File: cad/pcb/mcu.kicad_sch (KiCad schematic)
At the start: 30 parts, among them X3 SWD-Conn, Y1 32.768k, Y2 32MHz

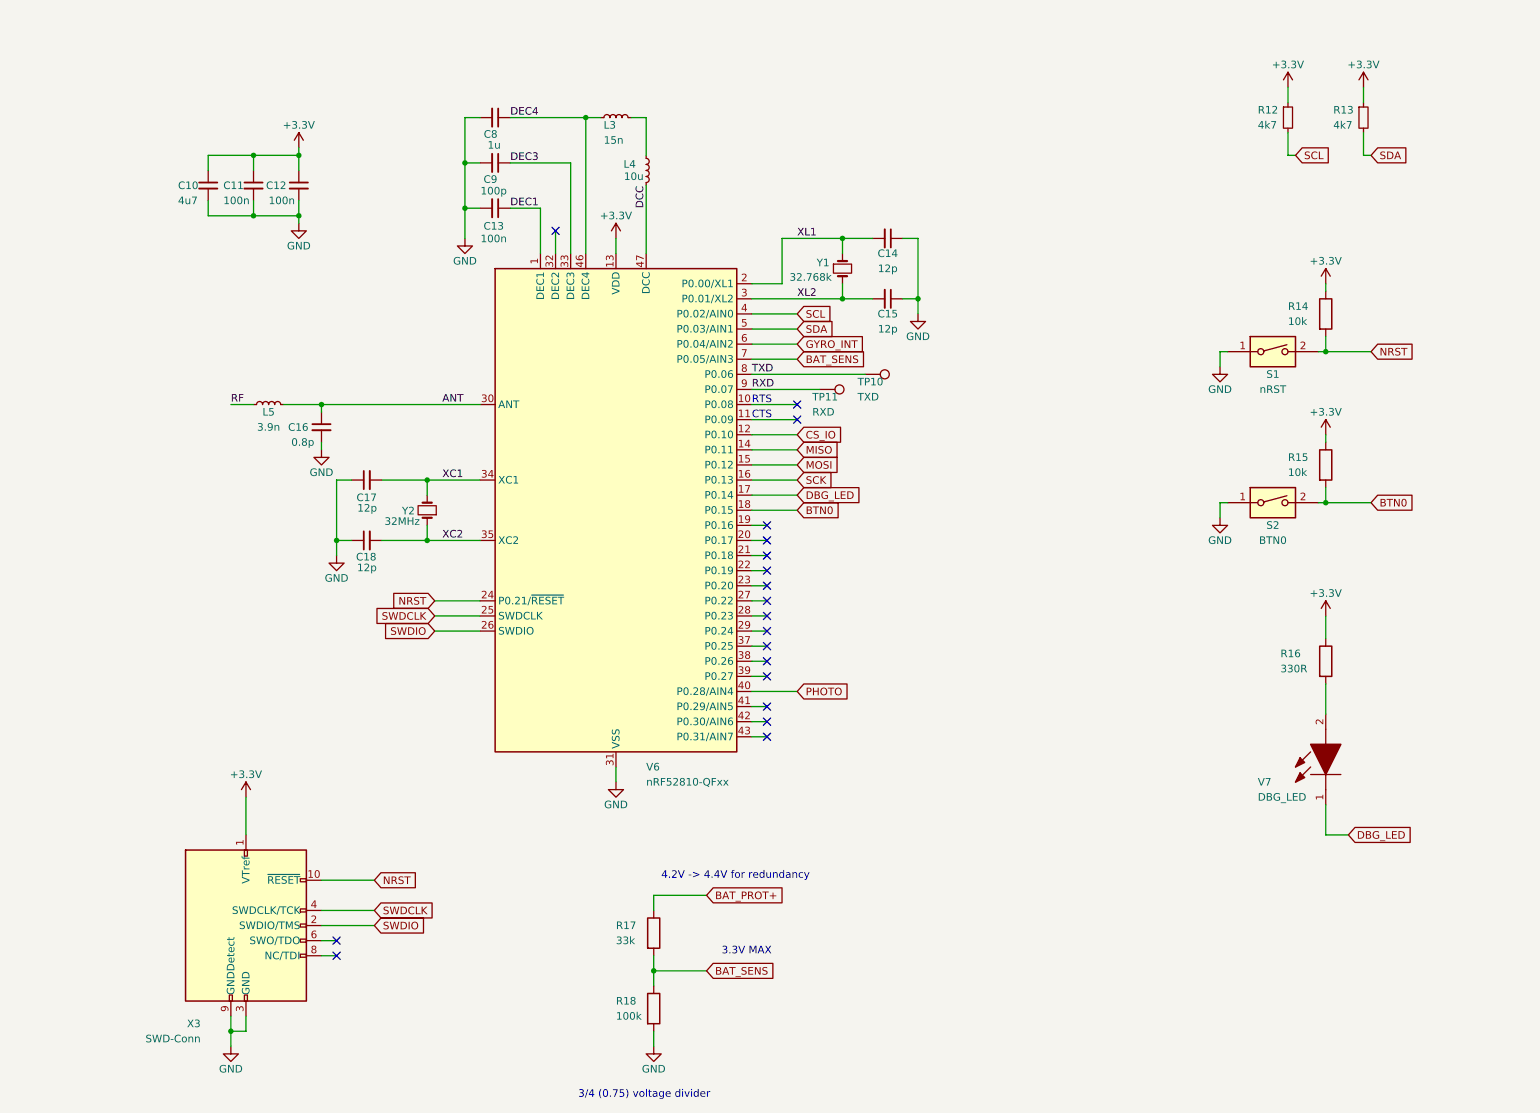
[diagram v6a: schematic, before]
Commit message: add usb-c footprint
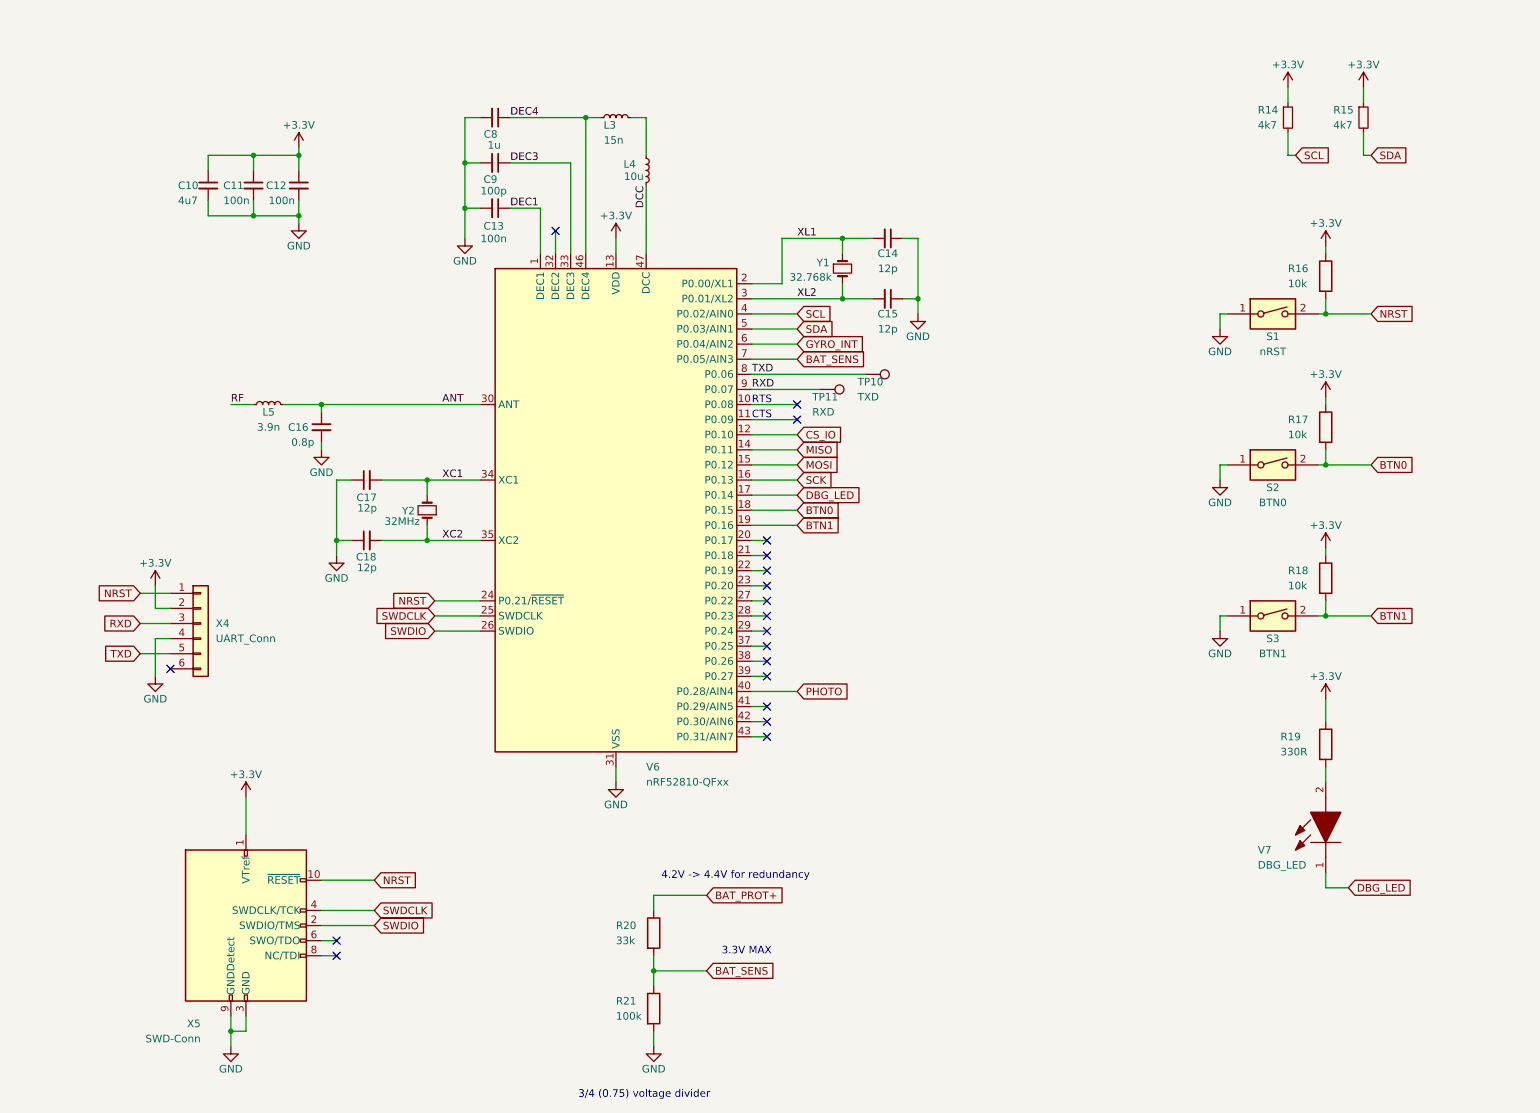
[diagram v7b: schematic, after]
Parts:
- added R18: 10k, symbol Device:R
- added S3: BTN1, symbol Switch:SW_DIP_x01
- added X4: UART_Conn, symbol Connector_Generic:Conn_01x06
- renumbered R12 to R14, R13 to R15, R14 to R16, R15 to R17, R16 to R19, R17 to R20, R18 to R21, X3 to X5
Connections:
- net +3.3V: now also R18.1, X4.2 (Pin_2)
- net GND: now also S3.1, X4.4 (Pin_4)
- net NRST: now also X4.1 (Pin_1)
- net RXD: now also X4.3 (Pin_3)
- net TXD: now also X4.5 (Pin_5)
- net BTN1: now reaches V6.19 (P0.16)
- net BTN1: now also R18.2, S3.2
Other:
- moved on the sheet: R16, R17, R19, S1, S2, V7

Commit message: generate bom; select C's & L's
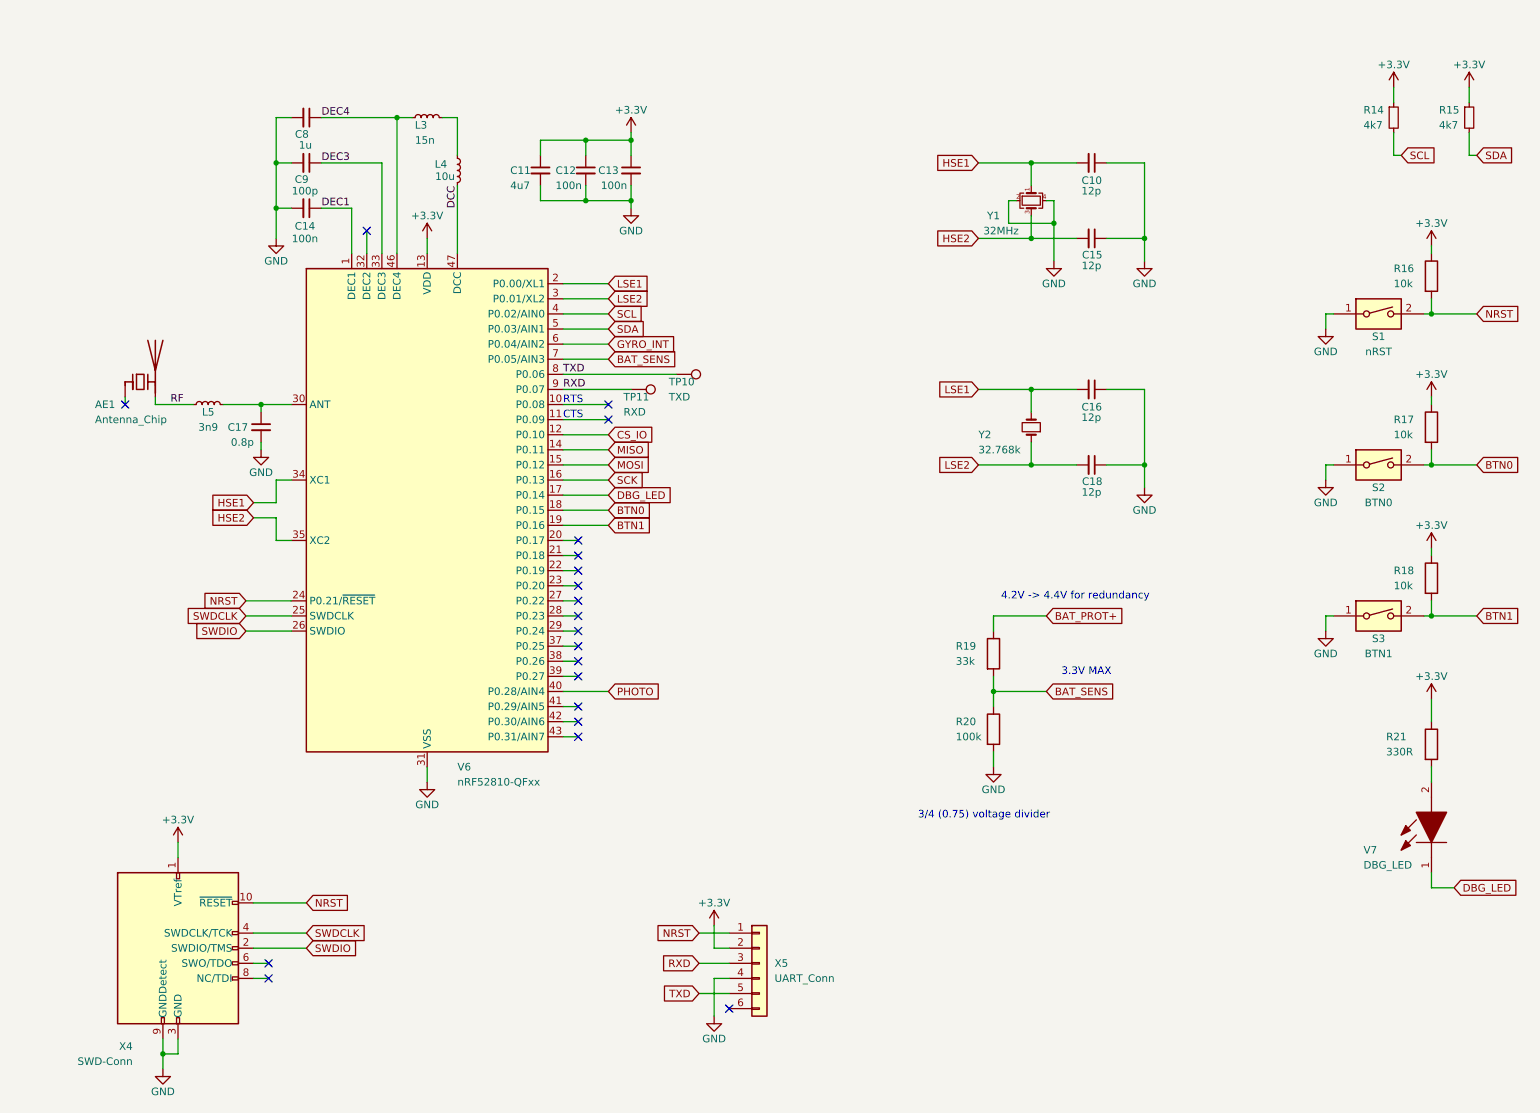
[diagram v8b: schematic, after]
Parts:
- removed C14, C17: 12p, symbol Device:C_Small
- removed Y1: 32.768k, symbol Device:Crystal_Small
- added AE1: Antenna_Chip, myLib:Ignion_NN01-102_BT_WIFI, symbol Device:Antenna_Chip
- added C10, C16: 12p, Capacitor_SMD:C_0603_1608Metric, symbol Device:C_Small
- added Y1: 32MHz, Crystal:Crystal_SMD_2520-4Pin_2.5x2.0mm, symbol Device:Crystal_GND24_Small
- C11: renamed from C10; footprint (none) -> Capacitor_SMD:C_0603_1608Metric
- C12: renamed from C11; footprint (none) -> Capacitor_SMD:C_0603_1608Metric
- C13: renamed from C12; footprint (none) -> Capacitor_SMD:C_0603_1608Metric
- C14: renamed from C13; footprint (none) -> Capacitor_SMD:C_0603_1608Metric
- C15, C18, C8, C9: footprint (none) -> Capacitor_SMD:C_0603_1608Metric
- C17: renamed from C16; footprint (none) -> Capacitor_SMD:C_0603_1608Metric
- L3, L4: footprint (none) -> Inductor_SMD:L_0603_1608Metric
- L5: value 3.9n -> 3n9; footprint (none) -> Inductor_SMD:L_0603_1608Metric
- R14, R15, R16, R17, R18: footprint (none) -> Resistor_SMD:R_0603_1608Metric
- R19: renamed from R20; footprint (none) -> Resistor_SMD:R_0603_1608Metric
- R20: renamed from R21; footprint (none) -> Resistor_SMD:R_0603_1608Metric
- R21: renamed from R19; footprint (none) -> Resistor_SMD:R_0603_1608Metric
- S1, S2, S3: footprint (none) -> Button_Switch_SMD:SW_SPST_CK_RS282G05A3
- TP10, TP11: footprint (none) -> TestPoint:TestPoint_Pad_D1.0mm
- V6: Mouser Part Number (none) -> 949-NRF52810-QFAA-T
- X5: renamed from X4; footprint (none) -> Connector_PinHeader_1.27mm:PinHeader_2x03_P1.27mm_Vertical_SMD
- Y2: value 32MHz -> 32.768k; footprint (none) -> Crystal:Crystal_SMD_3215-2Pin_3.2x1.5mm; Mouser Part Number (none) -> ECS-.327-9-34B-C-TR
- renumbered X5 to X4
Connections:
- net GND: now also C10.1, C16.1, Y1.2, Y1.4
- net RF: now also AE1.2 (PCB_Trace)
- net ANT: no longer names the net of C17.1, L5.2, V6.30 (ANT)
- net XC1 renamed HSE1
- net HSE1: now also C10.2, Y1.1; no longer Y2.2
- net XC2 renamed LSE2
- net LSE2: now also V6.3 (P0.01/XL2); no longer V6.35 (XC2)
- net XL1 renamed LSE1
- net LSE1: now also Y2.2, C16.2
- net XL2 renamed HSE2
- net HSE2: now also V6.35 (XC2), Y1.3; no longer V6.3 (P0.01/XL2)
- no-connect marks 19 -> 20
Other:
- moved on the sheet: C11, C12, C13, C14, C17, C8, C9, L3, L4, L5, R14, R15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
